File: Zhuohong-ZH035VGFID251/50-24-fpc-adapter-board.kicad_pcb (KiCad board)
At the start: 4 copper layers, 28.8 x 25.2 mm, 19 parts, among them J1 1-1734248-5, J2 10051922-2010ELF, SW1 SMD-BUTTON_4P-5.2X5.2X1.5MM-S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, U1 RS3236-1.8FY5, U3 AP3127B

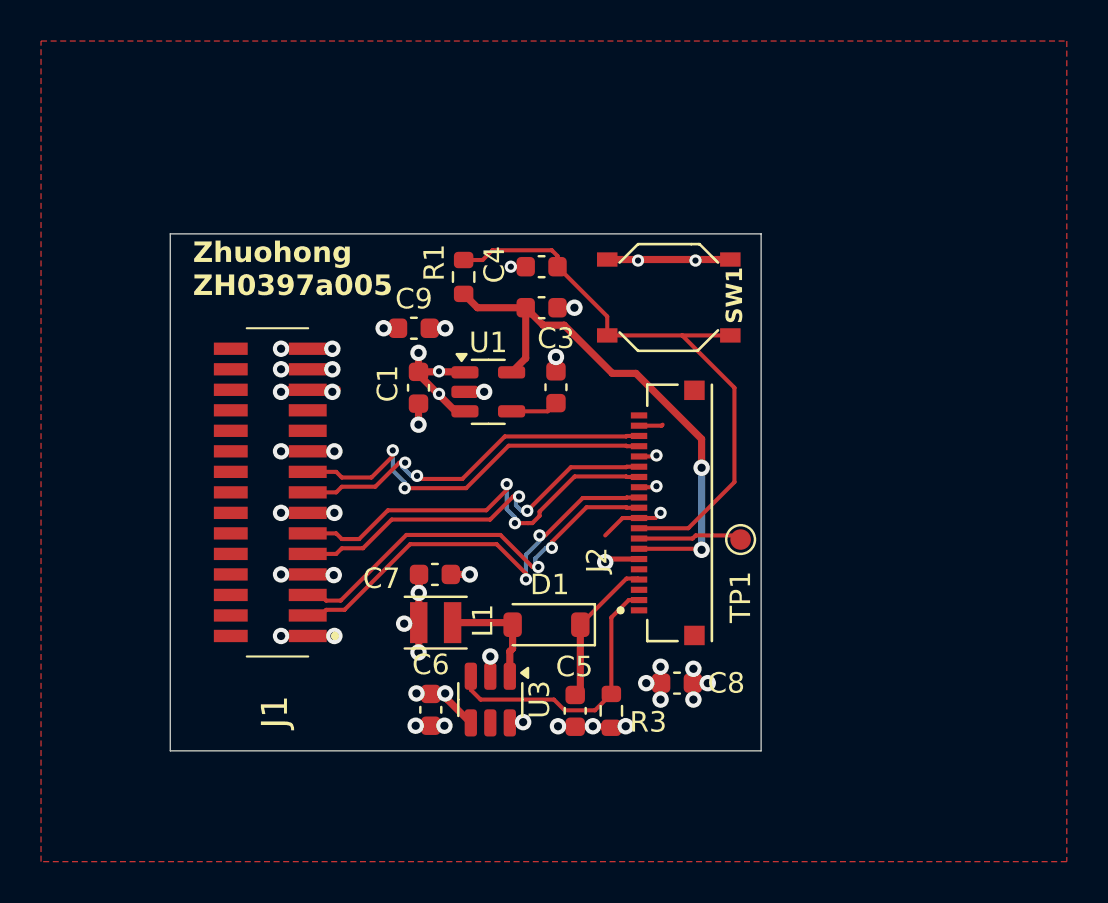
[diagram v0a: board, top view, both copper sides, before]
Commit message: Fix names, footprints, and silkscreen of the pcb's
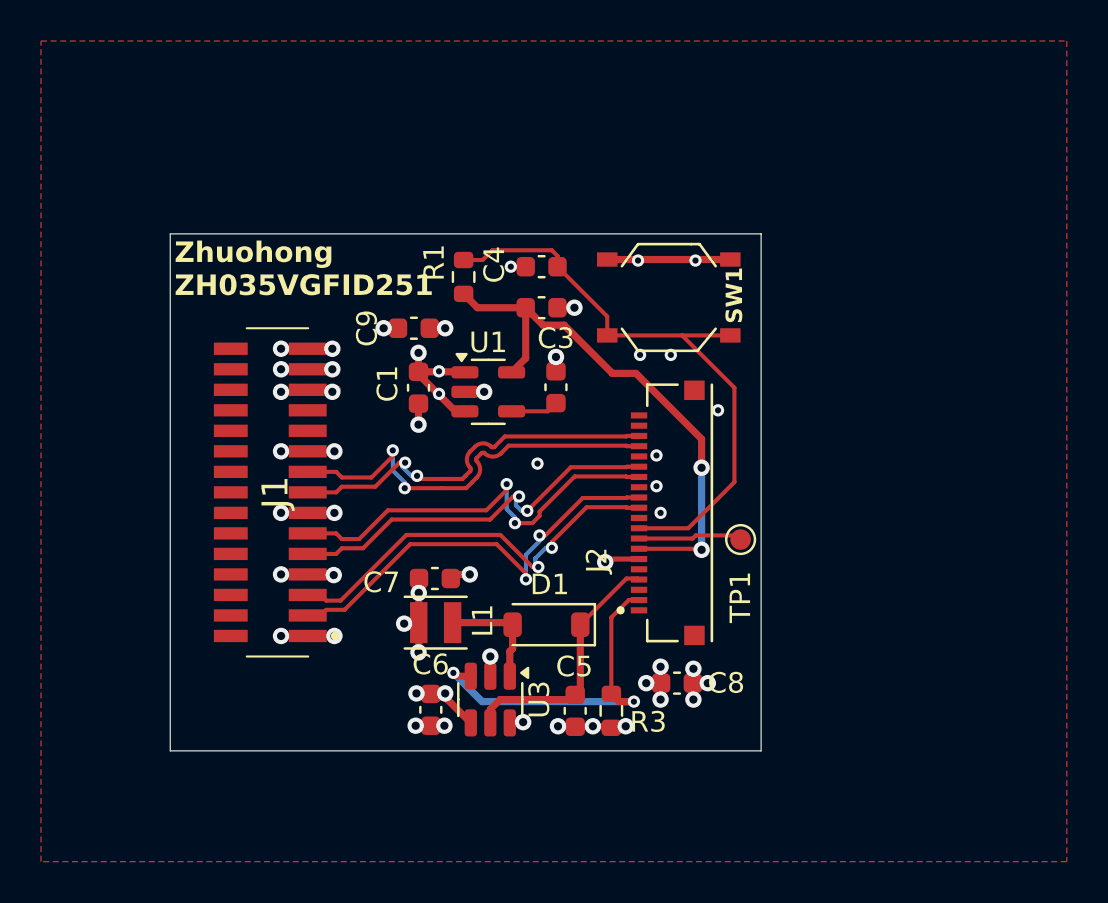
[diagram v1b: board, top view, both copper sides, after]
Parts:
- moved C7 0.20 mm to (79.2, 66.2)
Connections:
- U3 pad 5: (no net) -> LEDA
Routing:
- net GND: track 39.3 -> 20.2 mm, vias 31 -> 35
- net LEDA: track 6.99 -> 12.1 mm
- net LEDK: track 13.7 -> 17.0 mm, vias 0 -> 2
- net D0_P: track 19.3 -> 20.1 mm
- net D0_N: track 18.3 -> 19.0 mm
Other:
- board text added: "Zhuohong ZH035VGFID251"
- board text removed: "Zhuohong ZH0397a005"
